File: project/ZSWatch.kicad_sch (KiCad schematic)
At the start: 34 parts, among them IC1 nPM1300-QEXX, IC2 TS3USB221A, IC3 AT25SL128A, M1 NORA-B106, X1 DOCK, X2 INT, X3 VBAT, X4 VBUS, X5 SEL, X6 3V3

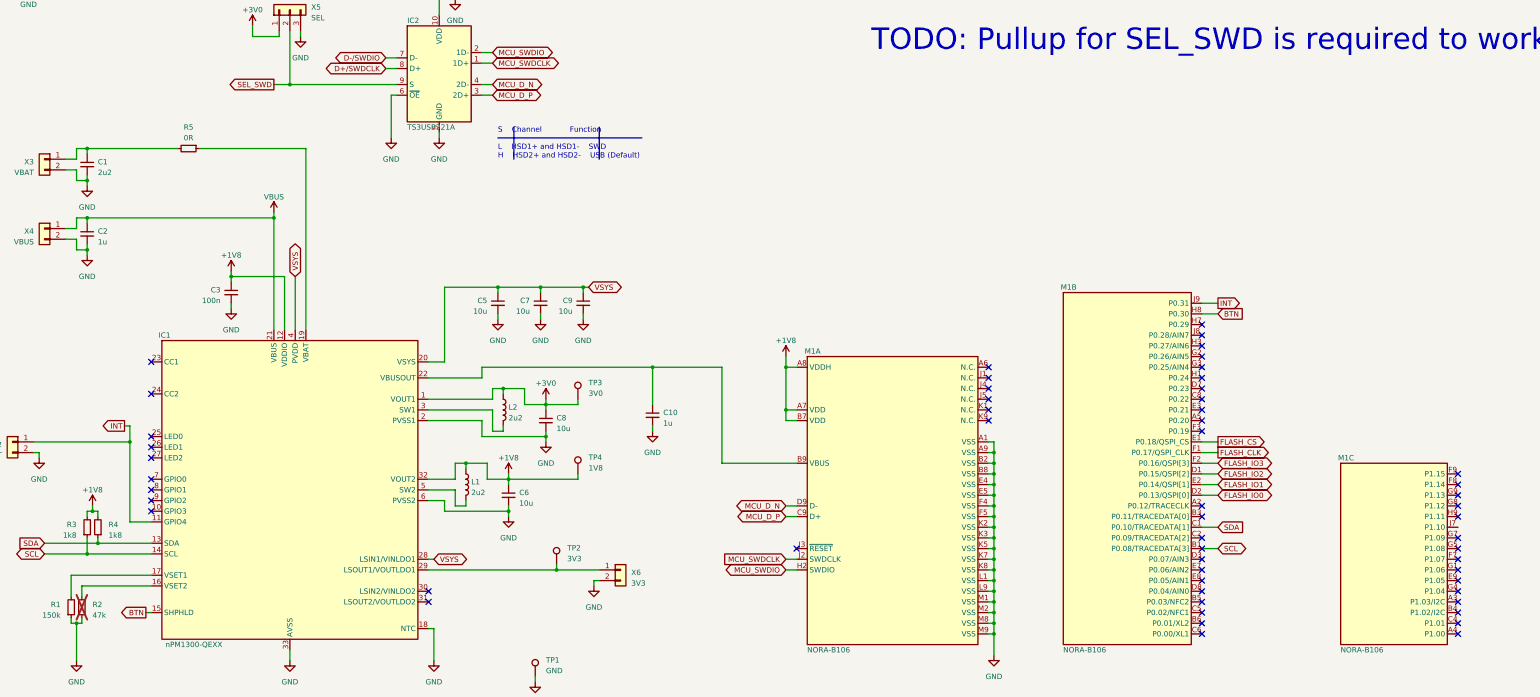
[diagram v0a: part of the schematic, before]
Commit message: VSET resistors need fix
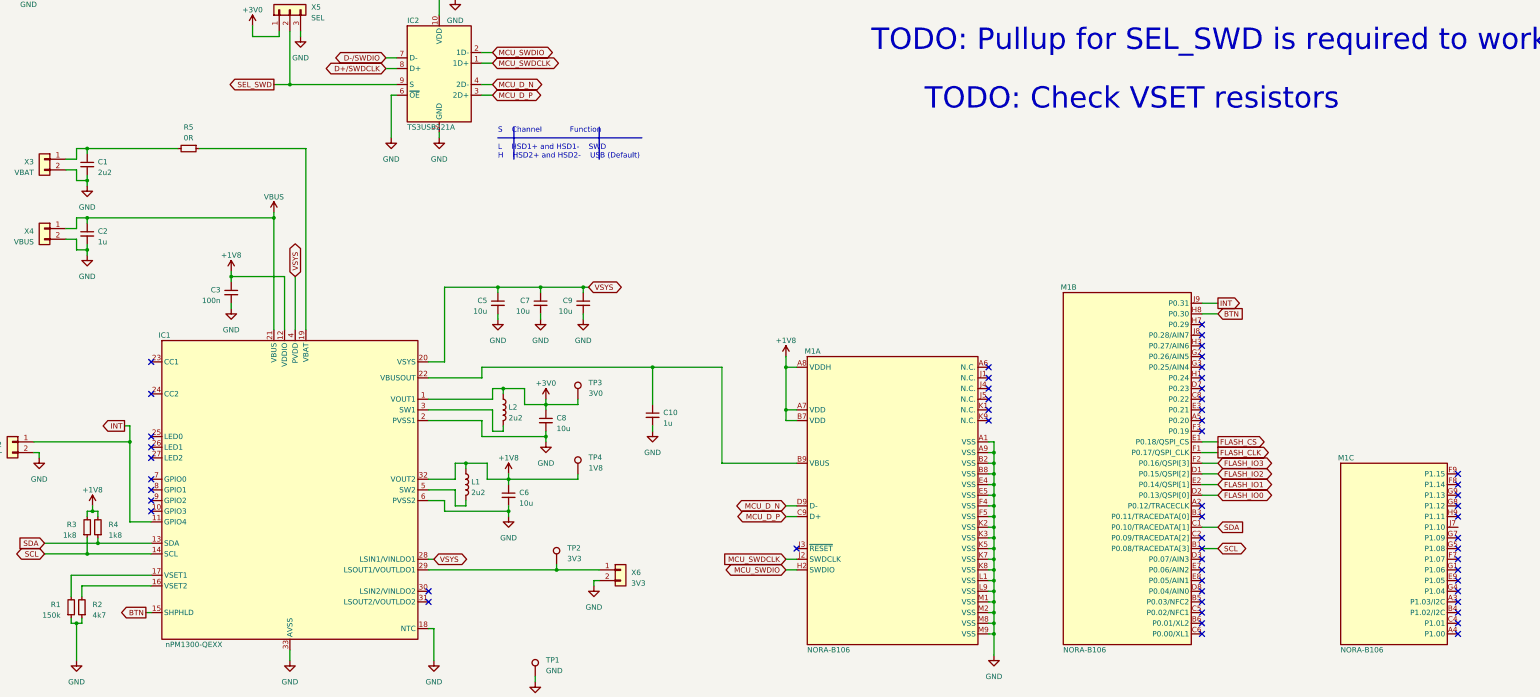
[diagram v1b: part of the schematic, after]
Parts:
- R2: value 47k -> 4k7; Mfr. No. RC0603FR-0747KL -> RC0603FR-074K7L; Order Number 603-RC0603FR-0747KL -> 603-RC0603FR-074K7L; now fitted; now in the parts list
- R3: Mfr. Vishay / Dale -> (none); Mfr. No. CRCW060311K8FKEA -> (none); Order Number 71-CRCW0603-11.8K-E3 -> (none)
- R4: Distributor Mouser -> (none); Mfr. Vishay / Dale -> (none); Mfr. No. CRCW060311K8FKEA -> (none); Order Number 71-CRCW0603-11.8K-E3 -> (none)
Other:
- note added: "TODO: Check VSET resistors"
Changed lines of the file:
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@@
+    (effects (font (size 5.08 5.08)) (justify left bottom))
+  )
+  (text "TODO: Check VSET resistors" (at 240.03 58.42 0)
     (effects (font (size 5.08 5.08)) (justify left bottom))
   )
@@
   )
   (symbol (lib_id "Device:R_Small") (at 39.37 176.53 180) (unit 1)
-    (in_bom no) (on_board yes) (dnp yes)
+    (in_bom yes) (on_board yes) (dnp no)
     (property "Reference" "R2" (at 41.91 175.895 0)
       (effects (font (size 1.27 1.27)) (justify right))
     )
-    (property "Value" "47k" (at 41.91 178.435 0)
+    (property "Value" "4k7" (at 41.91 178.435 0)
       (effects (font (size 1.27 1.27)) (justify right))
     )
@@
       (effects (font (size 1.27 1.27)) hide)
     )
-    (property "Mfr. No." "RC0603FR-0747KL" (at 39.37 176.53 0)
-      (effects (font (size 1.27 1.27)) hide)
-    )
-    (property "Order Number" "603-RC0603FR-0747KL" (at 39.37 176.53 0)
+    (property "Mfr. No." "RC0603FR-074K7L" (at 39.37 176.53 0)
+      (effects (font (size 1.27 1.27)) hide)
+    )
+    (property "Order Number" "603-RC0603FR-074K7L" (at 39.37 176.53 0)
       (effects (font (size 1.27 1.27)) hide)
     )
@@
       (effects (font (size 1.27 1.27)) hide)
     )
-    (property "Datasheet" "https://www.vishay.com/doc?20035" (at 40.64 157.48 0)
+    (property "Datasheet" "" (at 40.64 157.48 0)
       (effects (font (size 1.27 1.27)) hide)
     )
@@
       (effects (font (size 1.27 1.27)) hide)
     )
-    (property "Mfr." "Vishay / Dale" (at 40.64 157.48 0)
-      (effects (font (size 1.27 1.27)) hide)
-    )
-    (property "Mfr. No." "CRCW060311K8FKEA" (at 40.64 157.48 0)
-      (effects (font (size 1.27 1.27)) hide)
-    )
-    (property "Order Number" "71-CRCW0603-11.8K-E3" (at 40.64 157.48 0)
+    (property "Mfr." "" (at 40.64 157.48 0)
+      (effects (font (size 1.27 1.27)) hide)
+    )
+    (property "Mfr. No." "" (at 40.64 157.48 0)
+      (effects (font (size 1.27 1.27)) hide)
+    )
+    (property "Order Number" "" (at 40.64 157.48 0)
       (effects (font (size 1.27 1.27)) hide)
     )
@@
       (effects (font (size 1.27 1.27)) hide)
     )
-    (property "Datasheet" "https://www.vishay.com/doc?20035" (at 43.18 157.48 0)
-      (effects (font (size 1.27 1.27)) hide)
-    )
-    (property "Distributor" "Mouser" (at 43.18 157.48 0)
-      (effects (font (size 1.27 1.27)) hide)
-    )
-    (property "Mfr." "Vishay / Dale" (at 43.18 157.48 0)
-      (effects (font (size 1.27 1.27)) hide)
-    )
-    (property "Mfr. No." "CRCW060311K8FKEA" (at 43.18 157.48 0)
-      (effects (font (size 1.27 1.27)) hide)
-    )
-    (property "Order Number" "71-CRCW0603-11.8K-E3" (at 43.18 157.48 0)
-      (effects (font (size 1.27 1.27)) hide)
-    )
+    (property "Datasheet" "" (at 43.18 157.48 0)
+      (effects (font (size 1.27 1.27)) hide)
+    )
+    (property "Distributor" "" (at 43.18 157.48 0)
+      (effects (font (size 1.27 1.27)) hide)
+    )
+    (property "Mfr." "" (at 43.18 157.48 0)
+      (effects (font (size 1.27 1.27)) hide)
+    )
+    (property "Mfr. No." "" (at 43.18 157.48 0)
+      (effects (font (size 1.27 1.27)) hide)
+    )
+    (property "Order Number" "" (at 43.18 157.48 0)
+      (effects (font (size 1.27 1.27)) hide)
+    )

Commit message: Working on nPM circuit
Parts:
- R1: value 150k -> 47k; Mfr. No. RC0603FR-07150KL -> (none); Order Number 603-RC0603FR-07150KL -> (none)
- R2: value 4k7 -> 150k; Mfr. No. RC0603FR-074K7L -> (none); Order Number 603-RC0603FR-074K7L -> (none)
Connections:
- net +1V8: now also TP3.1; no longer TP4.1
- net +3V0: now also TP4.1; no longer TP3.1
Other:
- note removed: "TODO: Check VSET resistors"
- moved on the sheet: TP3, TP4
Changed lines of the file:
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@@
   (title_block
     (title "ZSWatch v2")
-    (date "2023-08-19")
+    (date "2023-10-26")
     (rev "3")
     (company "github.com/jakkra/ZSWatch-HW")
@@
     (effects (font (size 5.08 5.08)) (justify left bottom))
   )
-  (text "TODO: Check VSET resistors" (at 240.03 58.42 0)
-    (effects (font (size 5.08 5.08)) (justify left bottom))
-  )
   (global_label "BTN" (shape output) (at 31.75 311.15 0) (fields_autoplaced)
     (effects (font (size 1.27 1.27)) (justify left))
@@
       (effects (font (size 1.27 1.27)) (justify right))
     )
-    (property "Value" "150k" (at 34.29 178.435 0)
+    (property "Value" "47k" (at 34.29 178.435 0)
       (effects (font (size 1.27 1.27)) (justify right))
     )
@@
       (effects (font (size 1.27 1.27)) hide)
     )
-    (property "Mfr. No." "RC0603FR-07150KL" (at 36.83 176.53 0)
+    (property "Mfr. No." "" (at 36.83 176.53 0)
       (effects (font (size 1.27 1.27)) hide)
     )
-    (property "Order Number" "603-RC0603FR-07150KL" (at 36.83 176.53 0)
+    (property "Order Number" "" (at 36.83 176.53 0)
       (effects (font (size 1.27 1.27)) hide)
     )
@@
       (effects (font (size 1.27 1.27)) (justify right))
     )
-    (property "Value" "4k7" (at 41.91 178.435 0)
+    (property "Value" "150k" (at 41.91 178.435 0)
       (effects (font (size 1.27 1.27)) (justify right))
     )
@@
       (effects (font (size 1.27 1.27)) hide)
     )
-    (property "Mfr. No." "RC0603FR-074K7L" (at 39.37 176.53 0)
+    (property "Mfr. No." "" (at 39.37 176.53 0)
       (effects (font (size 1.27 1.27)) hide)
     )
-    (property "Order Number" "603-RC0603FR-074K7L" (at 39.37 176.53 0)
+    (property "Order Number" "" (at 39.37 176.53 0)
       (effects (font (size 1.27 1.27)) hide)
     )
@@
     )
   )
-  (symbol (lib_id "Connector:TestPoint") (at 157.48 127 0) (unit 1)
+  (symbol (lib_id "Connector:TestPoint") (at 157.48 144.78 0) (unit 1)
     (in_bom no) (on_board yes) (dnp no) (fields_autoplaced)
-    (property "Reference" "TP3" (at 160.02 123.063 0)
+    (property "Reference" "TP3" (at 160.02 140.843 0)
       (effects (font (size 1.27 1.27)) (justify left))
     )
-    (property "Value" "3V0" (at 160.02 125.603 0)
+    (property "Value" "3V0" (at 160.02 143.383 0)
       (effects (font (size 1.27 1.27)) (justify left))
     )
-    (property "Footprint" "TestPoint:TestPoint_Pad_1.0x1.0mm" (at 162.56 127 0)
+    (property "Footprint" "TestPoint:TestPoint_Pad_1.0x1.0mm" (at 162.56 144.78 0)
       (effects (font (size 1.27 1.27)) hide)
     )
-    (property "Datasheet" "~" (at 162.56 127 0)
+    (property "Datasheet" "~" (at 162.56 144.78 0)
       (effects (font (size 1.27 1.27)) hide)
     )
-    (property "Mfr." "" (at 157.48 127 0)
+    (property "Mfr." "" (at 157.48 144.78 0)
       (effects (font (size 1.27 1.27)) hide)
     )
-    (property "Mfr. No." "" (at 157.48 127 0)
+    (property "Mfr. No." "" (at 157.48 144.78 0)
       (effects (font (size 1.27 1.27)) hide)
     )
-    (property "Distributor" "" (at 157.48 127 0)
+    (property "Distributor" "" (at 157.48 144.78 0)
       (effects (font (size 1.27 1.27)) hide)
     )
-    (property "Order Number" "" (at 157.48 127 0)
+    (property "Order Number" "" (at 157.48 144.78 0)
       (effects (font (size 1.27 1.27)) hide)
     )
@@
     )
   )
-  (symbol (lib_id "Connector:TestPoint") (at 157.48 144.78 0) (unit 1)
+  (symbol (lib_id "Connector:TestPoint") (at 157.48 127 0) (unit 1)
     (in_bom no) (on_board yes) (dnp no) (fields_autoplaced)
-    (property "Reference" "TP4" (at 160.02 140.843 0)
+    (property "Reference" "TP4" (at 160.02 123.063 0)
       (effects (font (size 1.27 1.27)) (justify left))
     )
-    (property "Value" "1V8" (at 160.02 143.383 0)
+    (property "Value" "1V8" (at 160.02 125.603 0)
       (effects (font (size 1.27 1.27)) (justify left))
     )
-    (property "Footprint" "TestPoint:TestPoint_Pad_1.0x1.0mm" (at 162.56 144.78 0)
+    (property "Footprint" "TestPoint:TestPoint_Pad_1.0x1.0mm" (at 162.56 127 0)
       (effects (font (size 1.27 1.27)) hide)
     )
-    (property "Datasheet" "~" (at 162.56 144.78 0)
+    (property "Datasheet" "~" (at 162.56 127 0)
       (effects (font (size 1.27 1.27)) hide)
     )
-    (property "Mfr." "" (at 157.48 144.78 0)
+    (property "Mfr." "" (at 157.48 127 0)
       (effects (font (size 1.27 1.27)) hide)
     )
-    (property "Mfr. No." "" (at 157.48 144.78 0)
+    (property "Mfr. No." "" (at 157.48 127 0)
       (effects (font (size 1.27 1.27)) hide)
     )
-    (property "Distributor" "" (at 157.48 144.78 0)
+    (property "Distributor" "" (at 157.48 127 0)
       (effects (font (size 1.27 1.27)) hide)
     )
-    (property "Order Number" "" (at 157.48 144.78 0)
+    (property "Order Number" "" (at 157.48 127 0)
       (effects (font (size 1.27 1.27)) hide)
     )
